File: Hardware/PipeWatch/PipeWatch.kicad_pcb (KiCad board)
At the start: 2 copper layers, 96.5 x 100 mm, 50 parts, among them J1 WJ126V-5.0-2P, J2 A02YYUW, J3 Taster, U1 IRM-10-5_C20618064, U3 ESP32-S3-WROOM-1-N16R8, U4 LIS3DHTR_C15134, U5 XIAO-ESP32-S3-DIP, U6 ADS1115IDGS, U7 DS18B20, U8 DS18B20

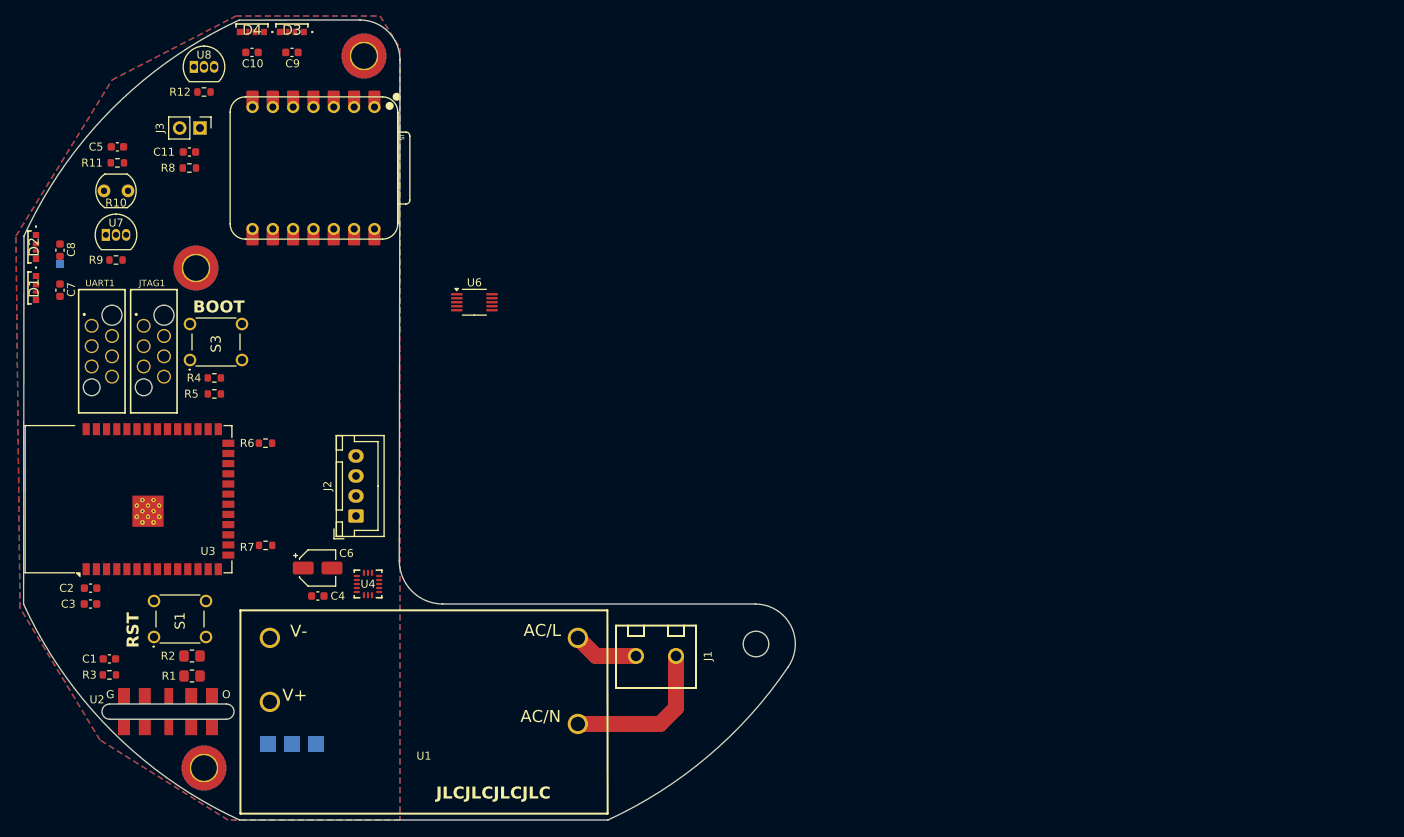
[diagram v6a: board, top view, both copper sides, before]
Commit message: Started laying traces
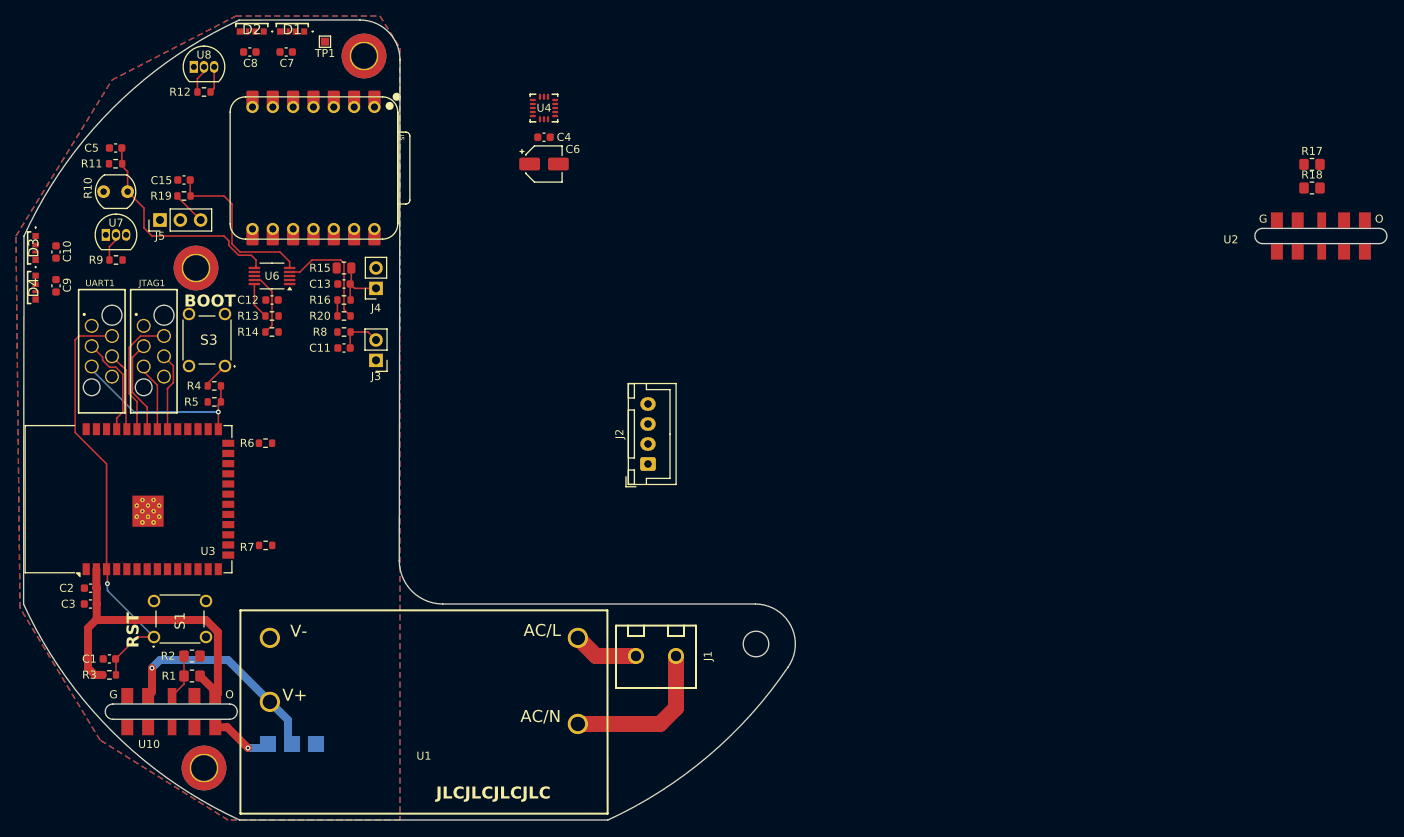
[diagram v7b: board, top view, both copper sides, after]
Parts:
- added C12: 100n, Capacitor_SMD:C_0603_1608Metric, F.Cu at (121.0, 85.0)
- added C13: 10n, Capacitor_SMD:C_0603_1608Metric, F.Cu at (130.0, 83.0)
- added C15: 10n, Capacitor_SMD:C_0603_1608Metric, F.Cu at (110.0, 70.0)
- added J4: Tiefensensor, Connector_PinSocket_2.54mm:PinSocket_1x02_P2.54mm_Vertical, F.Cu at (134.0, 83.5)
- added J5: Roter, Connector_PinHeader_2.54mm:PinHeader_1x03_P2.54mm_Vertical, F.Cu at (107.0, 75.0)
- added R13: 10k, Resistor_SMD:R_0603_1608Metric, F.Cu at (121.0, 87.0)
- added R14: 10k, Resistor_SMD:R_0603_1608Metric, F.Cu at (121.0, 89.0)
- added R15: 150R, Resistor_SMD:R_0805_2012Metric, F.Cu at (130.0, 81.0)
- added R16: 10k, Resistor_SMD:R_0603_1608Metric, F.Cu at (130.0, 85.0)
- added R17: R, Resistor_SMD:R_0805_2012Metric_Pad1.20x1.40mm_HandSolder, F.Cu at (251.0, 68.0)
- added R18: R, Resistor_SMD:R_0805_2012Metric_Pad1.20x1.40mm_HandSolder, F.Cu at (251.0, 71.0)
- added R19: 1k, Resistor_SMD:R_0603_1608Metric, F.Cu at (110.0, 72.0)
- added R20: 10k, Resistor_SMD:R_0603_1608Metric, F.Cu at (130.0, 87.0)
- added U10: ~, Felix:VC-D-40-A, F.Cu at (100.2, 137.4)
- TP1: moved to F.Cu
- U2: footprint Library:VC-D-40-A -> Felix:VC-D-40-A
- moved U2 155.9 mm to (243.9, 78.0)
- moved C4 63.9 mm to (155.0, 64.7)
- moved U4 63.4 mm to (155.0, 61.0), turned to 180 degrees
- moved C6 57.9 mm to (155.0, 68.0)
- moved D1 45.3 mm to (123.5, 51.4), turned to 180 degrees
- moved TP1 43.2 mm to (127.6, 52.7)
- moved D3 41.9 mm to (91.5, 78.5), turned to -90 degrees
- moved D4 41.9 mm to (91.5, 83.4), turned to -90 degrees
- moved C9 41.5 mm to (94.0, 83.2), turned to -90 degrees
- moved C7 41.1 mm to (122.8, 54.0), turned to 180 degrees
- moved D2 38.1 mm to (118.5, 51.4), turned to 180 degrees
- moved J2 37.1 mm to (168.0, 105.5)
- moved J3 36.4 mm to (134.0, 92.5), turned to 180 degrees
- moved C10 35.0 mm to (94.0, 79.0), turned to -90 degrees
- moved C8 34.3 mm to (118.2, 54.0), turned to 180 degrees
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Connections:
- C5 pad 2: /PhotowiederstandInnen/OUT -> /ADC/PhotowiederstandInnen/OUT
- R1 pad 2: Net-(U2-FB) -> Net-(U10-FB)
- R10 pad 2: /PhotowiederstandInnen/OUT -> /ADC/PhotowiederstandInnen/OUT
- R11 pad 1: /PhotowiederstandInnen/OUT -> /ADC/PhotowiederstandInnen/OUT
- R2 pad 1: Net-(U2-FB) -> Net-(U10-FB)
- U2 pad 3: Net-(U2-FB) -> unconnected-(U2-FB-Pad3)
- U2 pad 4: +3.3V -> unconnected-(U2-Vout-Pad4)
- U3 pad 25: unconnected-(U3-IO48-Pad25) -> /WS2812B3/Din
- U6 pad 1: unconnected-(U6-ADDR-Pad1) -> GND
- U6 pad 10: unconnected-(U6-SCL-Pad10) -> /ADC/SCL
- U6 pad 3: unconnected-(U6-GND-Pad3) -> GND
- U6 pad 4: unconnected-(U6-AIN0-Pad4) -> /ADC/Pressure/OUT
- U6 pad 5: unconnected-(U6-AIN1-Pad5) -> /ADC/Roter/OUT
- U6 pad 6: unconnected-(U6-AIN2-Pad6) -> /ADC/PhotowiederstandInnen/OUT
- U6 pad 8: unconnected-(U6-VDD-Pad8) -> +3.3V
- U6 pad 9: unconnected-(U6-SDA-Pad9) -> /ADC/SDA
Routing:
- net RST: track 0.00 -> 54.0 mm, vias 0 -> 1
- net +3.3V: track 0.00 -> 53.5 mm, vias 0 -> 1
- net /ADC/PhotowiederstandInnen/OUT: track 0.00 -> 28.2 mm
- net +5V: track 0.00 -> 27.4 mm, vias 0 -> 1
- net OI0: track 0.00 -> 24.0 mm, vias 0 -> 1
- net /ADC/Roter/OUT: track 0.00 -> 21.5 mm
- net MTMS: track 0.00 -> 15.6 mm
- net /ADC/Pressure/OUT: track 0.00 -> 14.5 mm
- net TX0: track 0.00 -> 12.8 mm
- net MTDI: track 0.00 -> 11.7 mm
- net RX0: track 0.00 -> 9.90 mm
- net MTCK: track 0.00 -> 9.90 mm
- net MTDO: track 0.00 -> 8.55 mm
- net /ADC/SDA: track 0.00 -> 8.20 mm
- net Net-(J4-Pin_1): track 0.00 -> 7.53 mm
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
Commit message: Final Version (Ordered it)
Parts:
- TP1: value Neopixel -> Neopxl
- moved R18 134.1 mm to (127.0, 122.0), turned to 180 degrees
- moved R17 134.1 mm to (127.0, 119.0)
- moved U2 118.6 mm to (133.9, 122.3), turned to 90 degrees
- moved C6 43.4 mm to (121.0, 95.0)
- moved U4 43.0 mm to (128.6, 95.0), turned to 0 degrees
- moved C4 43.0 mm to (121.0, 91.0)
- moved J2 34.3 mm to (133.9, 102.3), turned to 180 degrees
- moved R6 4.07 mm to (118.0, 99.5)
- moved C9 0.78 mm to (94.0, 84.0)
- moved R12 0.50 mm to (113.0, 59.0)
- moved C7 0.48 mm to (123.3, 53.9)
- moved D1 0.39 mm to (123.9, 51.4)
- moved D2 0.37 mm to (118.8, 51.4)
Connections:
- D4 pad 3: /WS2812B3/Din -> /WS2812B Data
- J2 pad 3: /A02YYUW/RX -> /Uart2_RX
- J2 pad 4: /A02YYUW/TX -> /Uart2_TX
- R13 pad 1: /ADC/SCL -> /ADC_SCL
- R14 pad 1: /ADC/SDA -> /ADC_SDA
- R17 pad 2: Net-(R17-Pad2) -> Net-(U2-FB)
- R18 pad 1: Net-(R17-Pad2) -> Net-(U2-FB)
- U2 pad 3: unconnected-(U2-FB-Pad3) -> Net-(U2-FB)
- U2 pad 4: unconnected-(U2-Vout-Pad4) -> +24V
- U3 pad 12: unconnected-(U3-IO8-Pad12) -> /Uart2_RX
- U3 pad 13: unconnected-(U3-IO19-Pad13) -> /Uart2_TX
- U3 pad 14: unconnected-(U3-IO20-Pad14) -> /TasterCall/OUT
- U3 pad 15: unconnected-(U3-IO3-Pad15) -> /MSU_INT1
- U3 pad 17: unconnected-(U3-IO9-Pad17) -> /MSU/INT2
- U3 pad 18: unconnected-(U3-IO10-Pad18) -> /MSU/CS
- U3 pad 19: unconnected-(U3-IO11-Pad19) -> /MSU/SAO
- U3 pad 20: unconnected-(U3-IO12-Pad20) -> /MSU/SDI
- U3 pad 21: unconnected-(U3-IO13-Pad21) -> /MSU/SPC
- U3 pad 22: unconnected-(U3-IO14-Pad22) -> /ADC_SDA
- U3 pad 23: unconnected-(U3-IO21-Pad23) -> /ADC_SCL
- U3 pad 24: unconnected-(U3-IO47-Pad24) -> Net-(U3-IO47)
- U3 pad 25: /WS2812B3/Din -> Net-(U3-IO48)
- U3 pad 31: unconnected-(U3-IO38-Pad31) -> /TemperaturOutside/OUT
- U3 pad 38: unconnected-(U3-IO2-Pad38) -> /TemperaturPipe/OUT
- U3 pad 39: unconnected-(U3-IO1-Pad39) -> /WS2812B Data
- U4 pad 11: /MSU/INT1 -> /MSU_INT1
- U5 pad 7: unconnected-(U5-U0TXD/D6/TX-Pad7) -> Net-(U3-IO47)
- U5 pad 8: unconnected-(U5-U0RXD/D7/RX-Pad8) -> Net-(U3-IO48)
- U6 pad 10: /ADC/SCL -> /ADC_SCL
- U6 pad 9: /ADC/SDA -> /ADC_SDA
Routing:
- net +3.3V: track 53.5 -> 271.0 mm, vias 1 -> 7
- net /TemperaturOutside/OUT: track 3.48 -> 55.8 mm, vias 0 -> 2
- net Net-(U3-IO47): track 0.00 -> 49.7 mm, vias 0 -> 1
- net GND: track 0.00 -> 45.7 mm, vias 0 -> 132
- net +24V: track 0.00 -> 43.7 mm
- net +5V: track 27.4 -> 69.0 mm, vias 1 -> 2
- net /TasterCall/OUT: track 5.61 -> 45.7 mm
- net /MSU_INT1: track 0.00 -> 34.9 mm, vias 0 -> 2
- net /ADC_SDA: track 0.00 -> 33.3 mm, vias 0 -> 2
- net /Uart2_RX: track 0.00 -> 31.5 mm
- net Net-(U3-IO48): track 0.00 -> 30.1 mm, vias 0 -> 1
- net /ADC_SCL: track 0.00 -> 29.3 mm, vias 0 -> 2
- net /MSU/INT2: track 0.00 -> 27.9 mm
- net /Uart2_TX: track 0.00 -> 27.3 mm
- net /MSU/CS: track 0.00 -> 26.3 mm
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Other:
- board text added: "L N"
